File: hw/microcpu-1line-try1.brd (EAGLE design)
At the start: 80 x 100 mm, 52 parts, among them IC1 IC_74HC595-TSSOP-16

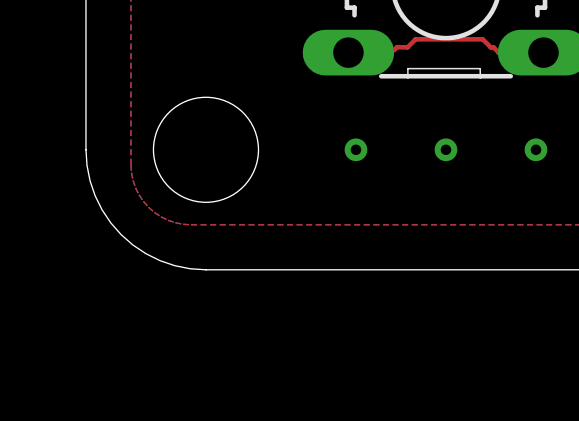
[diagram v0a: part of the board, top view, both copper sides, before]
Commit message: fixed for microcpu hardware, use fram
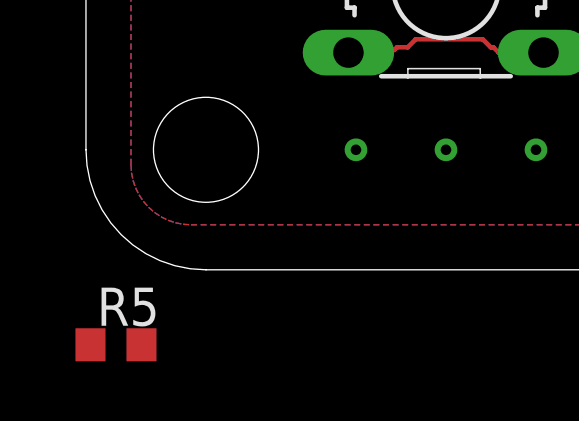
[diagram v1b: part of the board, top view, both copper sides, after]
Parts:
- added R5: 10K, resistor:R0603
- R10, R4, R9: value 10K -> 1K
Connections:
- new net N$5: R5.1, U1.3
- net VCC: now also R5.2
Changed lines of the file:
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@@
 <attribute name="NAME" x="28.155" y="52.415" size="1.27" layer="25" rot="R180"/>
 </element>
-<element name="R4" library="resistor" library_urn="urn:adsk.eagle:library:348" package="R0603" package3d_urn="urn:adsk.eagle:package:26057/1" value="10K" x="21.5" y="50" smashed="yes" rot="R270">
+<element name="R4" library="resistor" library_urn="urn:adsk.eagle:library:348" package="R0603" package3d_urn="urn:adsk.eagle:package:26057/1" value="1K" x="21.5" y="50" smashed="yes" rot="R270">
 <attribute name="NAME" x="22.135" y="51.135" size="1.27" layer="25" rot="R270"/>
 </element>
-<element name="R9" library="resistor" library_urn="urn:adsk.eagle:library:348" package="R0603" package3d_urn="urn:adsk.eagle:package:26057/1" value="10K" x="30" y="50" smashed="yes" rot="R270">
+<element name="R9" library="resistor" library_urn="urn:adsk.eagle:library:348" package="R0603" package3d_urn="urn:adsk.eagle:package:26057/1" value="1K" x="30" y="50" smashed="yes" rot="R270">
 <attribute name="NAME" x="30.635" y="51.135" size="1.27" layer="25" rot="R270"/>
 </element>
-<element name="R10" library="resistor" library_urn="urn:adsk.eagle:library:348" package="R0603" package3d_urn="urn:adsk.eagle:package:26057/1" value="10K" x="26" y="50" smashed="yes" rot="R90">
+<element name="R10" library="resistor" library_urn="urn:adsk.eagle:library:348" package="R0603" package3d_urn="urn:adsk.eagle:package:26057/1" value="1K" x="26" y="50" smashed="yes" rot="R90">
 <attribute name="NAME" x="25.365" y="48.365" size="1.27" layer="25" rot="R90"/>
 </element>
@@
 <attribute name="NAME" x="8.135" y="68.365" size="1.27" layer="26" rot="MR90"/>
 <attribute name="VALUE" x="5.595" y="68.365" size="1.27" layer="28" rot="MR90"/>
+</element>
+<element name="R5" library="resistor" library_urn="urn:adsk.eagle:library:348" package="R0603" package3d_urn="urn:adsk.eagle:package:26057/1" value="10K" x="1" y="-2.5" smashed="yes">
+<attribute name="NAME" x="0.365" y="-1.865" size="1.27" layer="25"/>
+<attribute name="VALUE" x="0.365" y="-4.405" size="1.27" layer="27"/>
 </element>
 </elements>
@@
 <wire x1="37.263375" y1="66.8277" x2="38.118875" y2="67.6832" width="0.2032" layer="16"/>
 <wire x1="10.31" y1="52.84" x2="12.85" y2="52.84" width="0.2032" layer="16"/>
+<contactref element="R5" pad="2"/>
+<wire x1="1.85" y1="-2.5" x2="10.31" y2="52.84" width="0" layer="19" extent="1-1"/>
 </signal>
 <signal name="TDO">
@@
 <wire x1="10.27525" y1="68.0847" x2="10.31" y2="68.08" width="0.1524" layer="16"/>
 </signal>
+<signal name="N$5">
+<contactref element="R5" pad="1"/>
+<contactref element="U1" pad="3"/>
+<wire x1="0.15" y1="-2.5" x2="47.45" y2="74.365" width="0" layer="19" extent="1-1"/>
+</signal>
 </signals>

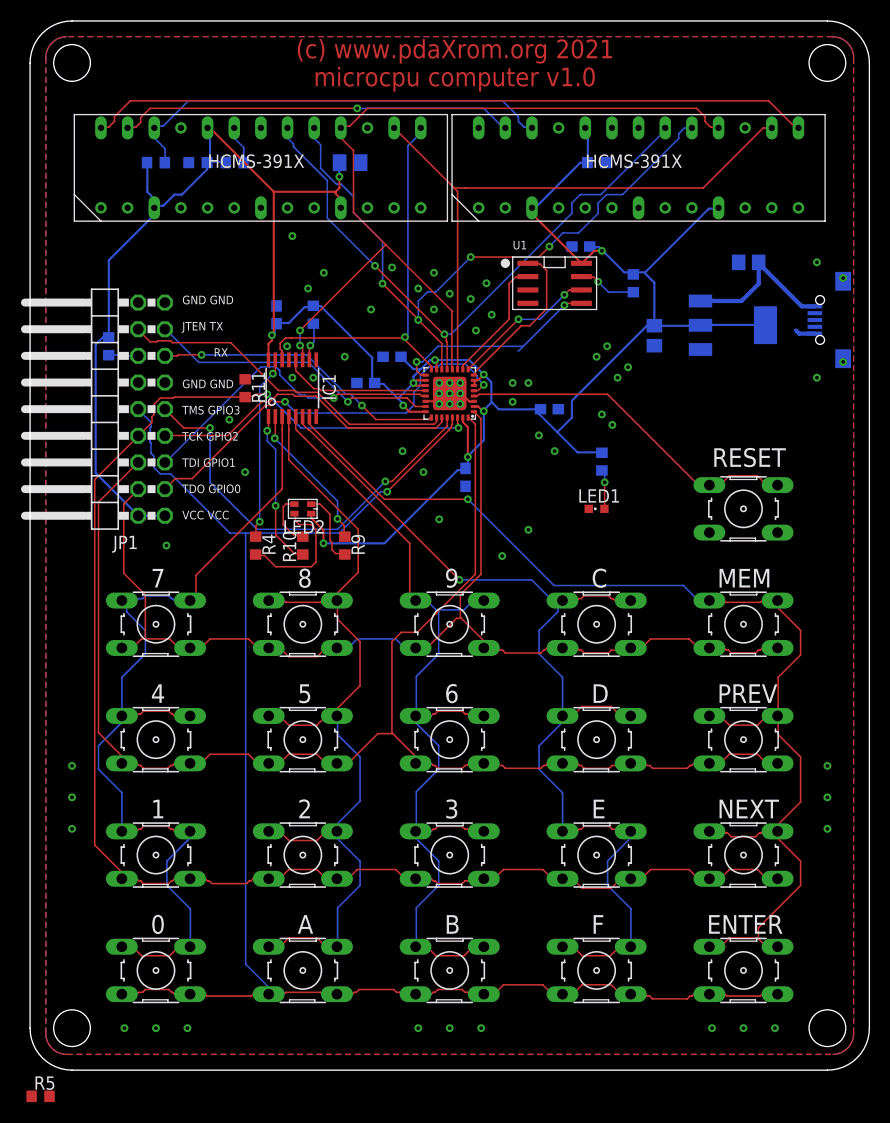
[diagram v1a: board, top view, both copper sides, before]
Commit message: wp pullup for fram, diodes for matrix keyboard
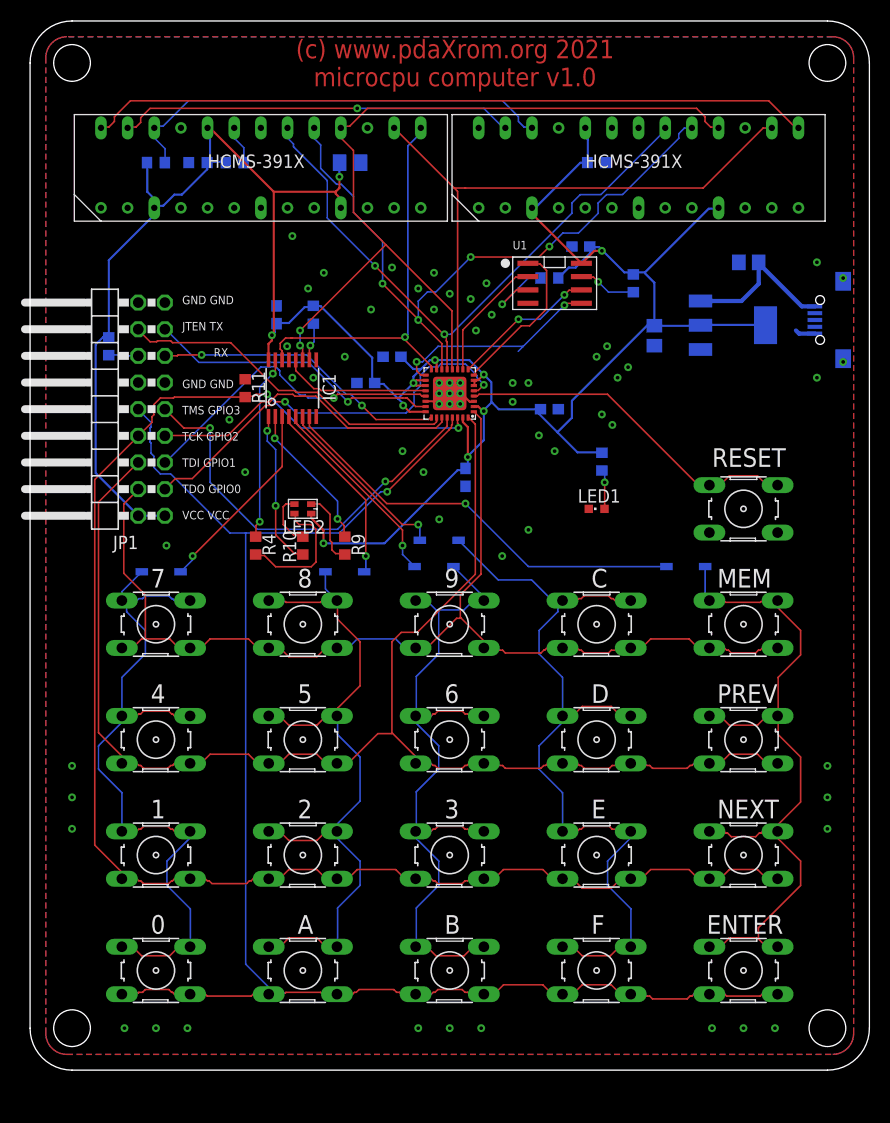
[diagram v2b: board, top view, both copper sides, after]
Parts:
- added D1, D2, D3, D4, D5: (no value), adafruit:SOD-123
- moved R5 91.8 mm to (49.5, 75.5), flipped to the bottom, turned to 180 degrees
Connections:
- new net N$13: D1.C, IC1.3
- new net N$14: D2.C, IC1.4
- new net N$15: D3.C, IC1.5
- new net N$16: D4.C, IC1.6
- new net N$17: D5.C, IC1.7
- net KC0: now also D1.A; no longer IC1.3
- net KC1: now also D2.A; no longer IC1.4
- net KC2: now also D3.A; no longer IC1.5
- net KC3: now also D4.A; no longer IC1.6
- net KC4: now also D5.A; no longer IC1.7
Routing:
- net KC4: track 112.4 -> 70.0 mm, vias 1 -> 0
- net N$17: track 0.00 -> 40.5 mm, vias 0 -> 1
- net KC3: track 99.5 -> 79.4 mm, vias 1 -> 0
- net N$15: track 0.00 -> 19.0 mm, vias 0 -> 1
- net N$13: track 0.00 -> 18.8 mm, vias 0 -> 1
- net KC1: track 88.0 -> 70.1 mm
- net N$14: track 0.00 -> 17.9 mm, vias 0 -> 1
- net KC2: track 87.3 -> 69.6 mm
- net KC0: track 87.9 -> 70.2 mm
- net N$16: track 0.00 -> 17.3 mm, vias 0 -> 1
- net N$5: track 0.00 -> 7.70 mm, vias 0 -> 1
- net VCC: track 244.2 -> 248.8 mm
